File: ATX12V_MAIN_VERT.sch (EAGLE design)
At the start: 7 parts, among them J1 ATX12V_MAIN_VERT, J2 1X12, J3 1X12, J4 1X04, J5 1X04, J6 1X04, J7 1X04

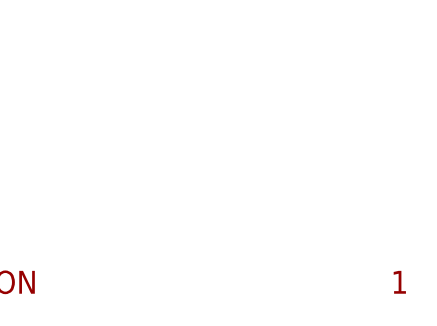
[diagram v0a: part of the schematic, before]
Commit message: Fix some silk screen flaws in pin header devices.
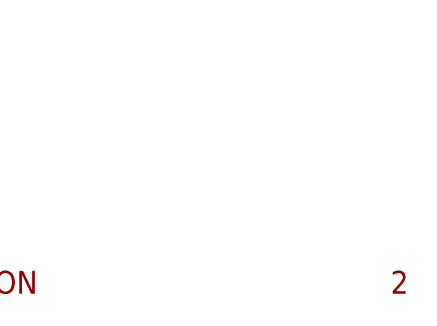
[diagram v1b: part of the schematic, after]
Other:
- note added: "2"
- note removed: "1"
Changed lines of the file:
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@@
 <plain>
 <text x="172.72" y="6.35" size="2.54" layer="94">ALAN JOHNSON</text>
-<text x="236.22" y="6.35" size="2.54" layer="94">1</text>
+<text x="236.22" y="6.35" size="2.54" layer="94">2</text>
 </plain>
 <instances>
